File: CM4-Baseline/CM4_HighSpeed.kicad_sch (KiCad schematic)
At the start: 5 parts, among them J10 690-019-298-412, U8 RT9742SNGV

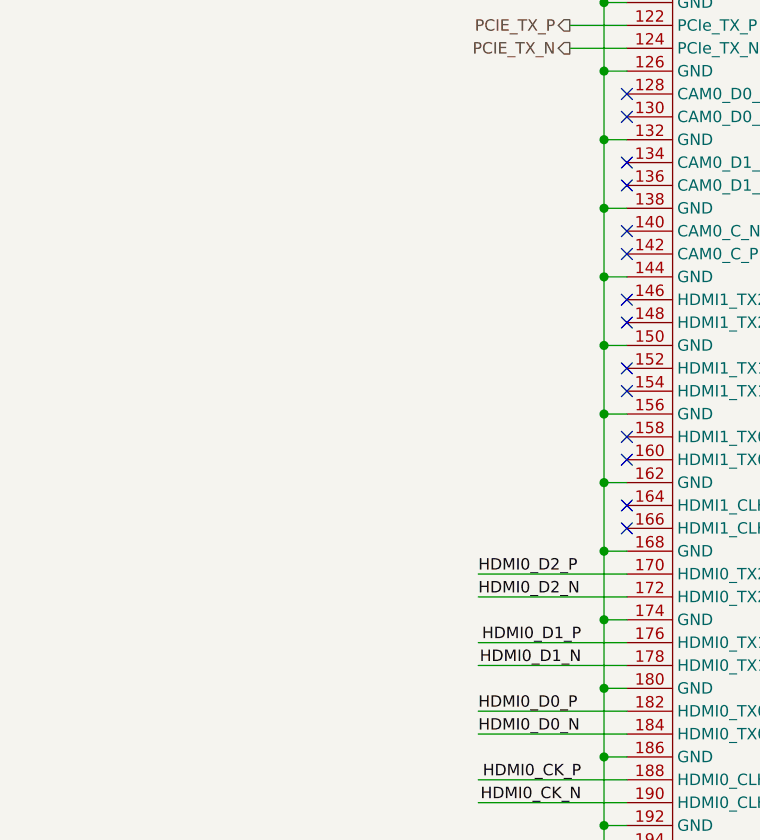
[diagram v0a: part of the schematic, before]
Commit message: Added CSI connector and associated library
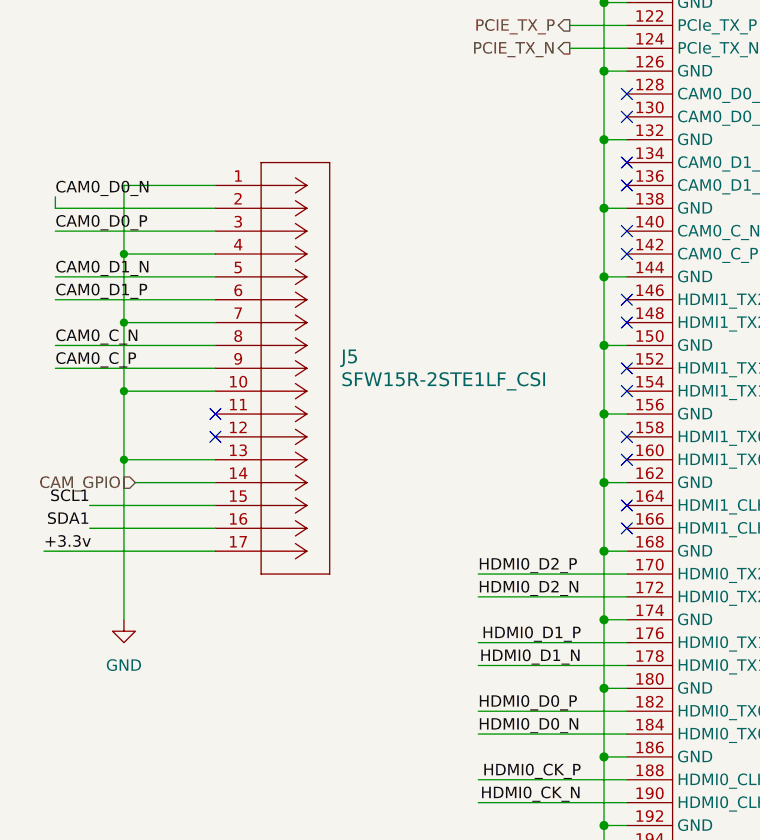
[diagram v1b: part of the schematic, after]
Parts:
- added J5: SFW15R-2STE1LF_CSI, CON15_1X15_DRB_SFW_FCI, symbol SFW15R-2STE1LF:SFW15R-2STE1LF
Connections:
- net GND: now also J5.1, J5.10, J5.13, J5.4, J5.7
- new net +3.3v: J5.17
- new net CAM0_C_N: J5.8
- new net CAM0_C_P: J5.9
- new net CAM0_D0_N: J5.2
- new net CAM0_D0_P: J5.3
- new net CAM0_D1_N: J5.5
- new net CAM0_D1_P: J5.6
- new net CAM_GPIO: J5.14
- new net SCL1: J5.15
- new net SDA1: J5.16
- no-connect marks 47 -> 49
